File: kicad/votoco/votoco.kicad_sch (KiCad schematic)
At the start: 100 parts, among them J1 Conn_01x04, J10 Conn_01x02, J11 Conn_01x02, J12 Conn_01x02, J13 Conn_01x02, J14 Conn_01x02, J15 Conn_01x02, J2 Conn_01x02, J3 Conn_01x04, J4 Conn_02x05_Odd_Even, J5 Conn_01x02, J6 Conn_01x03, J8 Conn_01x03, J9 USB_B_Micro, Q1 RQ6E045TN, Q2 RQ6E045TN, Q3 RQ6E045TN, SW1 Reset, SW2 Boot, U1 TMC2209-LA-T, U2 STM32F072CBUx, U3 SN65HVD231, U4 TMP112xxDRL, U5 MAX2040xAFL, U6 NCP1117-3.3, U7 ADXL345BCCZ, Y1 12Mhz

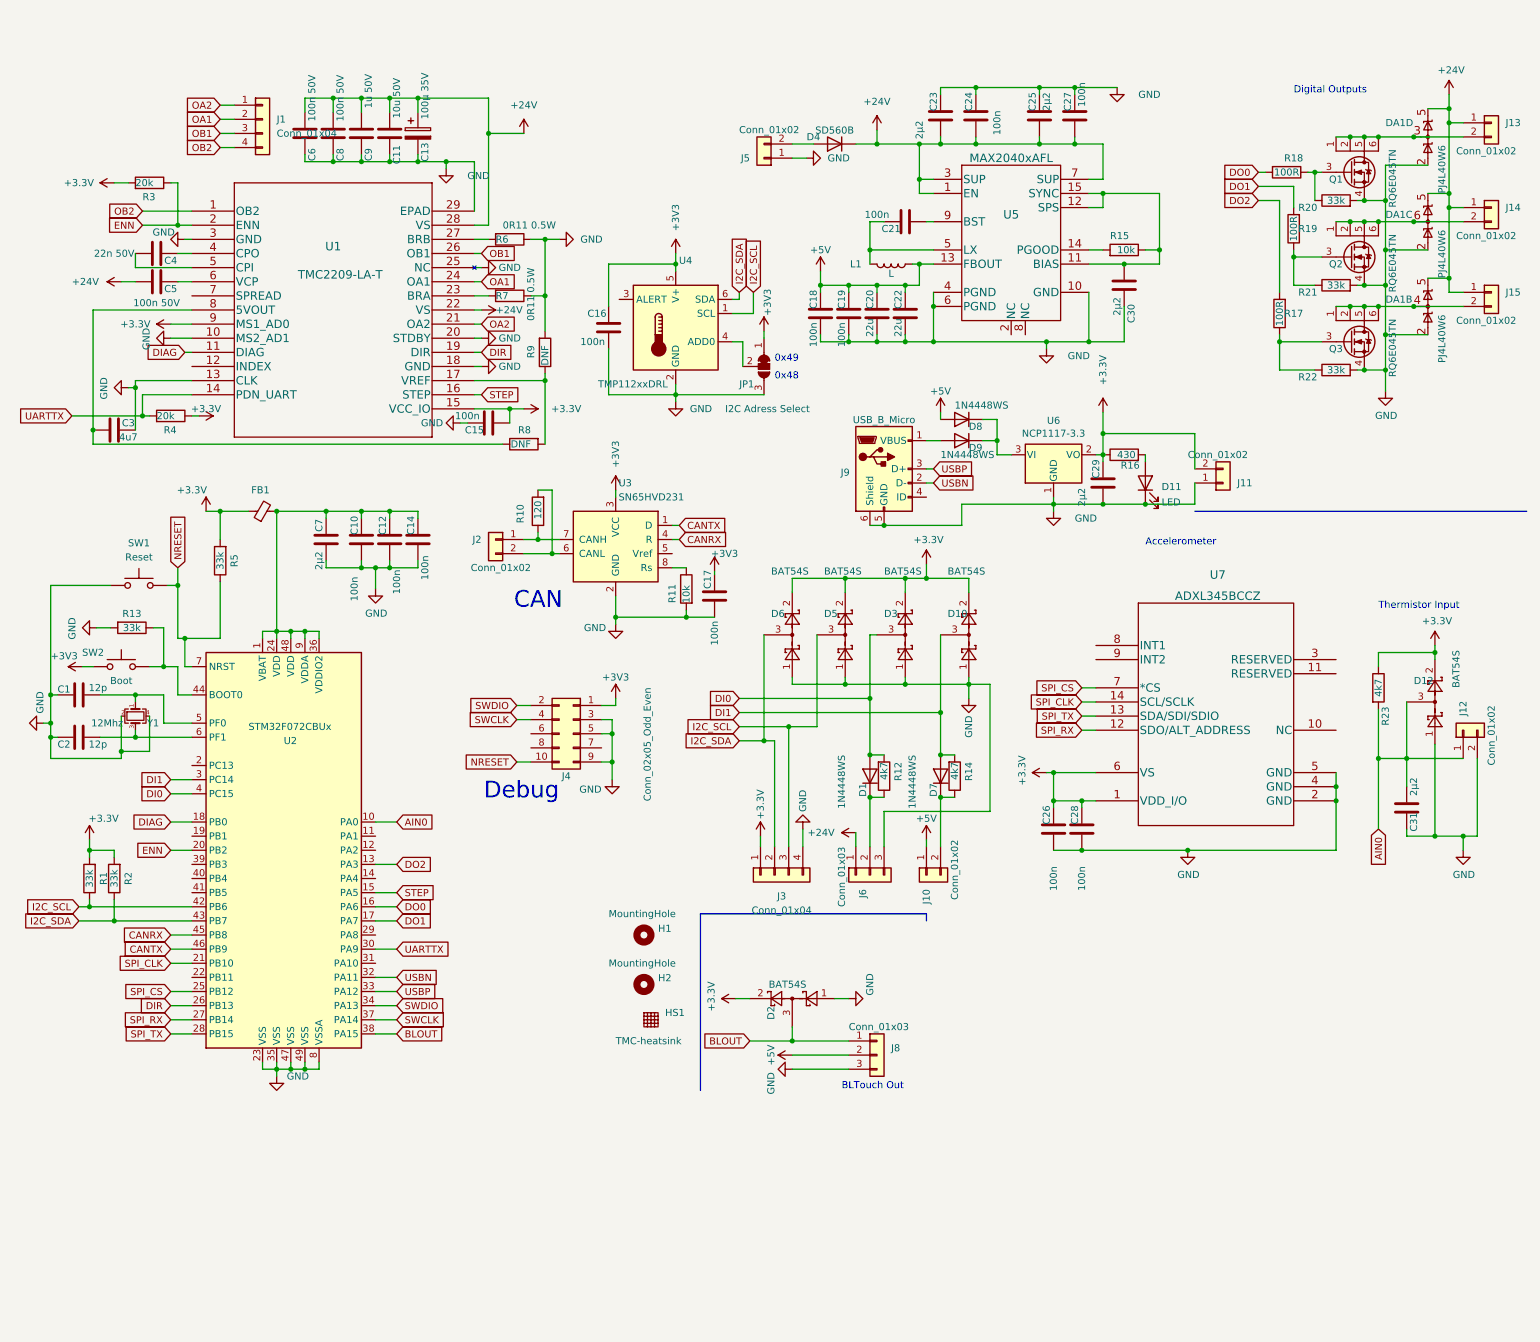
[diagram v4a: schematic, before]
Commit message: footprint corrected / DIR - SPI clk pins exchanged
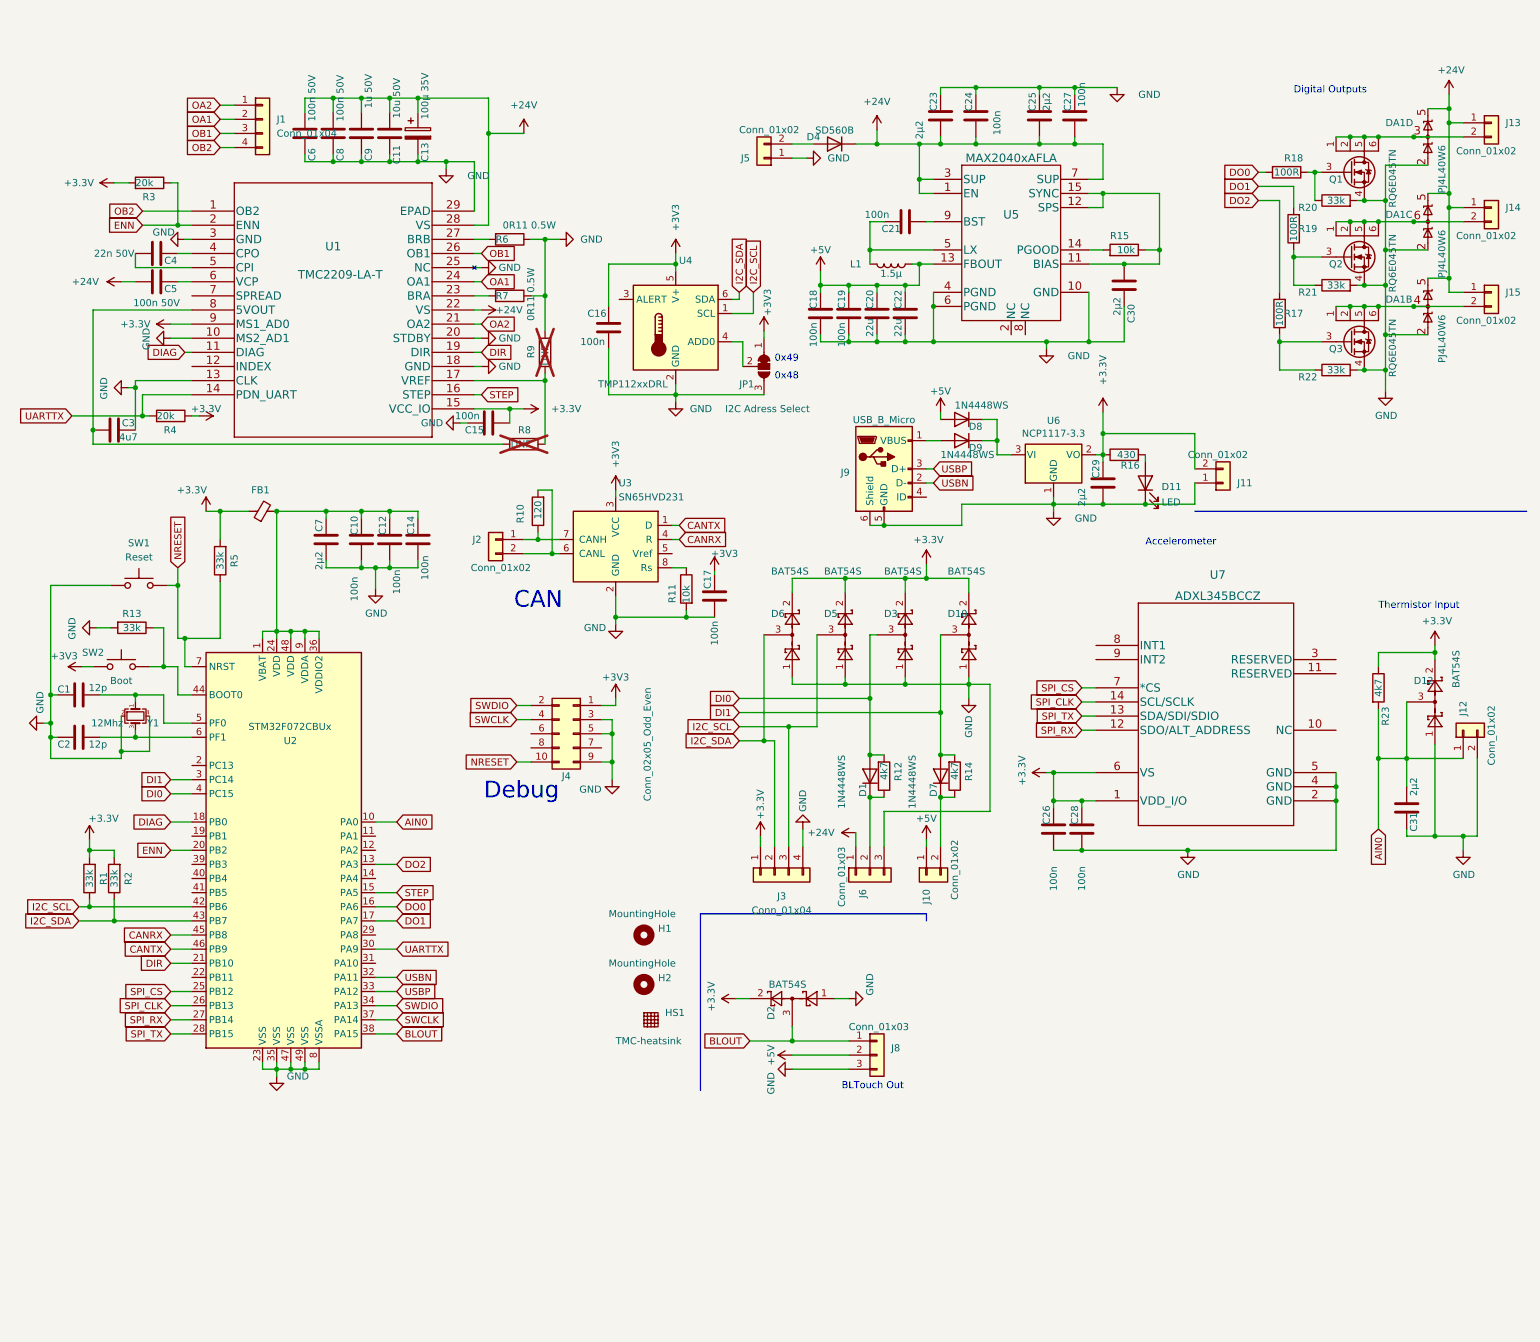
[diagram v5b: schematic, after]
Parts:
- C16: footprint Capacitor_SMD:C_0603_1608Metric_Pad1.08x0.95mm_HandSolder -> Capacitor_SMD:C_0603_1608Metric
- L1: value L -> 1.5µ
- R8, R9: now not fitted; now left out of the parts list
- U5: value MAX2040xAFL -> MAX2040xAFLA
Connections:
- net DIR: now also U2.21 (PB10); no longer U2.26 (PB13)
- net SPI_CLK: now also U2.26 (PB13); no longer U2.21 (PB10)
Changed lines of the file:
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@@
     )
   )
-  (global_label "DIR" (shape input) (at 40.64 181.61 180) (fields_autoplaced)
+  (global_label "DIR" (shape input) (at 40.64 173.99 180) (fields_autoplaced)
     (effects (font (size 1.27 1.27)) (justify right))
-    (property "Intersheetrefs" "${INTERSHEET_REFS}" (at 35.0821 181.5306 0)
+    (property "Intersheetrefs" "${INTERSHEET_REFS}" (at 35.0821 173.9106 0)
       (effects (font (size 1.27 1.27)) (justify right) hide)
     )
@@
     )
   )
-  (global_label "SPI_CLK" (shape input) (at 40.64 173.99 180) (fields_autoplaced)
+  (global_label "SPI_CLK" (shape input) (at 40.64 181.61 180) (fields_autoplaced)
     (effects (font (size 1.27 1.27)) (justify right))
-    (property "Intersheetrefs" "${INTERSHEET_REFS}" (at 30.1142 173.99 0)
+    (property "Intersheetrefs" "${INTERSHEET_REFS}" (at 30.1142 181.61 0)
       (effects (font (size 1.27 1.27)) (justify right) hide)
     )
@@
   )
   (symbol (lib_id "Device:R") (at 107.95 64.135 0) (mirror x) (unit 1)
-    (in_bom yes) (on_board yes) (dnp no)
+    (in_bom no) (on_board yes) (dnp yes)
     (property "Reference" "R9" (at 105.41 62.865 90)
       (effects (font (size 1.27 1.27)) (justify left))
@@
       (effects (font (size 1.27 1.27)))
     )
-    (property "Value" "L" (at 170.18 49.9594 90)
+    (property "Value" "1.5µ" (at 170.18 49.9594 90)
       (effects (font (size 1.27 1.27)))
     )
@@
       (effects (font (size 1.524 1.524)))
     )
-    (property "Value" "MAX2040xAFL" (at 191.77 29.21 0)
+    (property "Value" "MAX2040xAFLA" (at 191.77 29.21 0)
       (effects (font (size 1.524 1.524)))
     )
@@
       (effects (font (size 1.27 1.27)) (justify left))
     )
-    (property "Footprint" "Capacitor_SMD:C_0603_1608Metric_Pad1.08x0.95mm_HandSolder" (at 120.3452 63.5 0)
+    (property "Footprint" "Capacitor_SMD:C_0603_1608Metric" (at 120.3452 63.5 0)
       (effects (font (size 1.27 1.27)) hide)
     )
@@
   )
   (symbol (lib_id "Device:R") (at 104.14 80.645 90) (mirror x) (unit 1)
-    (in_bom yes) (on_board yes) (dnp no)
+    (in_bom no) (on_board yes) (dnp yes)
     (property "Reference" "R8" (at 105.41 78.105 90)
       (effects (font (size 1.27 1.27)) (justify left))
